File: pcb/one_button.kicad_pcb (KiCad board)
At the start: 2 copper layers, 47.8 x 61.3 mm, 62 parts, among them J1 DX07S016JA1R1500, J2 Conn_01x02, J3 Conn_01x06, SW1 R-667843, U1 ATmega32U4-A, U2 MIC5219-5.0YM5, U3 1SS400T1G, Y1 ECS-160-10-36-CKM-TR3

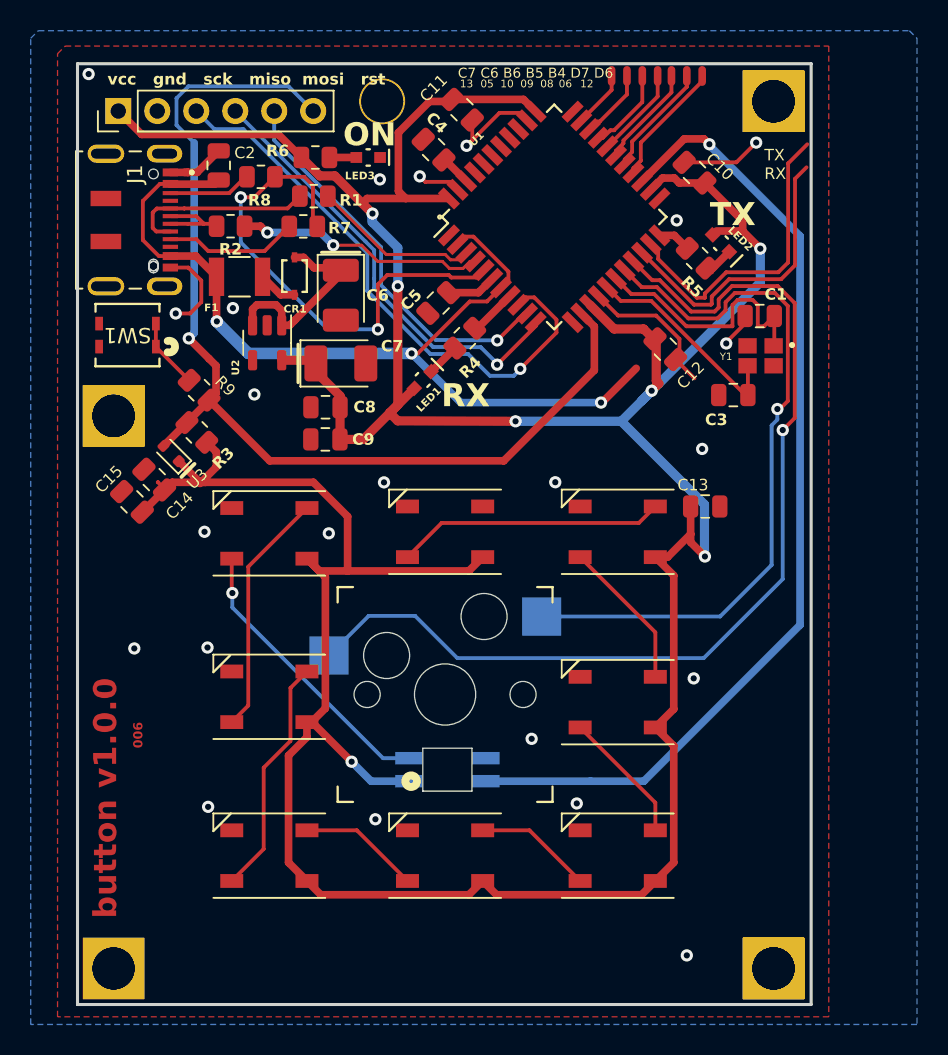
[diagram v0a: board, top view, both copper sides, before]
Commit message: fix pcb, firmware
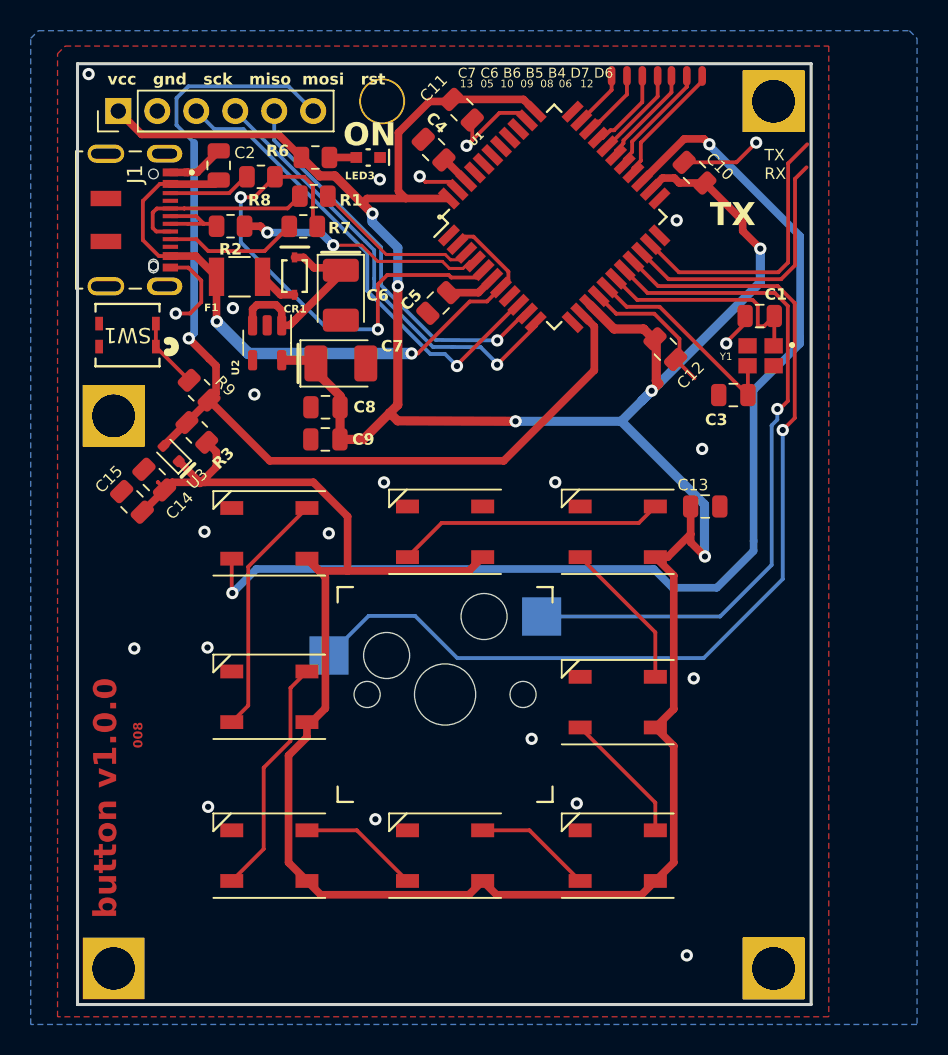
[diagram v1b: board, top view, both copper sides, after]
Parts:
- removed LED1, LED2: LTST-C191KSKT, footprints:LED_LTST-C191KRKT_LTO
- removed LED4: 4960, SK6812-E:4960_ADA
- removed R4, R5: 330, Resistor_SMD:R_0805_2012Metric
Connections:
- D7 pad 4: Net-(D7-DIN) -> D4
- U1 pad 22: Net-(U1-PD5) -> unconnected-(U1-PD5-Pad22)
- U1 pad 8: Net-(U1-PB0) -> unconnected-(U1-PB0-Pad8)
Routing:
- net Net-(D7-DIN): track 19.0 -> 0.00 mm, vias 1 -> 0
- net VBUS: track 60.8 -> 43.8 mm, vias 3 -> 2
- net VCC: track 253.7 -> 241.4 mm, vias 7 -> 6
- net D4: track 64.4 -> 74.7 mm, vias 1 -> 2
- net D15: track 37.5 -> 31.0 mm
- net Net-(U1-PB0): track 3.14 -> 0.00 mm
- net Net-(U1-XTAL1): track 16.9 -> 14.6 mm
- net Net-(LED1-Pad1): track 2.18 -> 0.00 mm
- net Net-(U1-PD5): track 2.16 -> 0.00 mm
- net TXO: track 20.0 -> 18.2 mm
- net Net-(LED2-Pad1): track 1.81 -> 0.00 mm
- net D3: track 47.4 -> 45.7 mm
- net D2: track 65.6 -> 63.9 mm
- net RXI: track 19.4 -> 17.8 mm
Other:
- board text added: "008"
- board text added: "r9"
- board text removed: "006"
- board text removed: "4960"
- board text removed: "RX"
- board text removed: "d1-d8"
- board text removed: "green"
- board text removed: "led1"
- board text removed: "led2"
- board text removed: "led3"
- board text removed: "led4"
- board text removed: "leds"
- board text removed: "r4-5, 9"
- board text removed: "red"
- board text removed: "ws2812b"
- board text removed: "yellow"
